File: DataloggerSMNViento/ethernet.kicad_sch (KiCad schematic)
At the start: 1 part

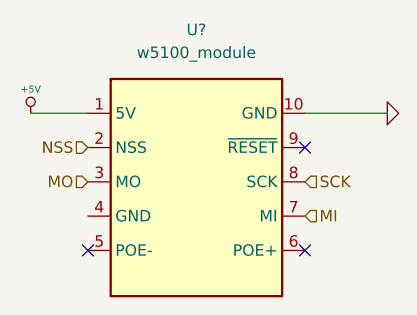
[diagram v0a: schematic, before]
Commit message: Agrego modificaciones al poncho de la EDU CIAA, también agrego una simulacion del circuito para tomar la tensión del ADC del tunnel
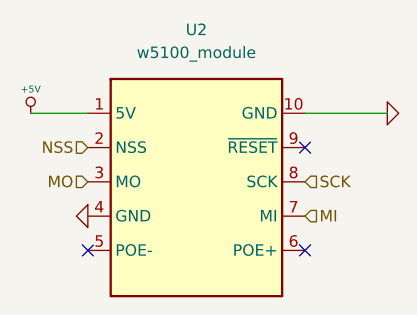
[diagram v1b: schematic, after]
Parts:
- U2: renamed from U?; footprint (none) -> Modulos:W5100_module
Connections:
- net GND: now also U2.4 (GND)
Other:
- company: (none) -> Servicio Meteorológico Nacional - FIUBA - UBA
- title: (none) -> Datalogger para SCTV
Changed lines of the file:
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@@
 (kicad_sch (version 20211123) (generator eeschema)
   (paper "A4")
+  (title_block
+    (title "Datalogger para SCTV")
+    (date "2023-10-20")
+    (rev "1.0")
+    (company "Servicio Meteorológico Nacional - FIUBA - UBA")
+    (comment 1 "poner repo")
+    (comment 2 "Autores y Licencia del poncho: Cristian Aranda (FIUBA), ver archivo licence.txt")
+    (comment 3 "Autor del poncho: Cristian Zozimo Aranda Cordero.  Ver directorio \"doc\"")
+    (comment 4 "CÓDIGO PONCHO: DT1")
+  )
   (no_connect (at 147.193 68.961))
   (no_connect (at 123.063 68.961))
@@
   (symbol (lib_id "Misc_Poncho_Grande:GND") (at 156.337 53.721 90) (unit 1)
     (in_bom yes) (on_board yes) (fields_autoplaced)
-    (property "Reference" "#PWR?" (id 0) (at 156.337 53.721 0)
+    (property "Reference" "#PWR014" (id 0) (at 156.337 53.721 0)
       (effects (font (size 0.762 0.762)) hide)
     )
@@
   (symbol (lib_id "New_Library:w5100_module") (at 134.493 76.581 0) (unit 1)
     (in_bom yes) (on_board yes) (fields_autoplaced)
-    (property "Reference" "U?" (id 0) (at 135.128 44.45 0))
+    (property "Reference" "U2" (id 0) (at 135.128 44.45 0))
     (property "Value" "w5100_module" (id 1) (at 135.128 46.99 0))
-    (property "Footprint" "" (id 2) (at 134.493 76.581 0)
+    (property "Footprint" "Modulos:W5100_module" (id 2) (at 134.493 76.581 0)
       (effects (font (size 1.27 1.27)) hide)
     )
@@
   (symbol (lib_id "Misc_Poncho_Grande:+5V") (at 116.713 53.721 0) (unit 1)
     (in_bom yes) (on_board yes) (fields_autoplaced)
-    (property "Reference" "#PWR?" (id 0) (at 116.713 51.435 0)
+    (property "Reference" "#PWR013" (id 0) (at 116.713 51.435 0)
       (effects (font (size 0.508 0.508)) hide)
     )
@@
       (effects (font (size 1.524 1.524)))
     )
+    (pin "1")
+  )
+  (symbol (lib_id "Misc_Poncho_Grande:GND") (at 123.063 65.151 270) (unit 1)
+    (in_bom yes) (on_board yes) (fields_autoplaced)
+    (property "Reference" "#PWR0102" (id 0) (at 123.063 65.151 0)
+      (effects (font (size 0.762 0.762)) hide)
+    )
+    (property "Value" "GND" (id 1) (at 121.285 65.151 0)
+      (effects (font (size 0.762 0.762)) hide)
+    )
+    (property "Footprint" "" (id 2) (at 123.063 65.151 0)
+      (effects (font (size 1.524 1.524)))
+    )
+    (property "Datasheet" "" (id 3) (at 123.063 65.151 0)
+      (effects (font (size 1.524 1.524)))
+    )

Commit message: Subo la version v1.0 del PCB del poncho de la tesis
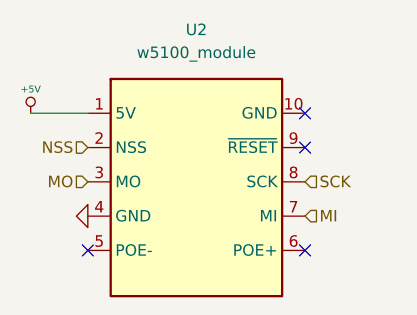
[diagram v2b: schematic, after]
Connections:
- net GND: no longer U2.10 (GND)
- no-connect marks 3 -> 4
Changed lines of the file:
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@@
   (no_connect (at 123.063 68.961))
   (no_connect (at 147.193 57.531))
-  (wire (pts (xy 147.193 53.721) (xy 156.337 53.721))
-    (stroke (width 0) (type default) (color 0 0 0 0))
-  )
+  (no_connect (at 147.193 53.721))
   (wire (pts (xy 116.713 53.721) (xy 123.063 53.721))
     (stroke (width 0) (type default) (color 0 0 0 0))
@@
     (effects (font (size 1.27 1.27)) (justify right))
   )
-  (symbol (lib_id "Misc_Poncho_Grande:GND") (at 156.337 53.721 90) (unit 1)
-    (in_bom yes) (on_board yes) (fields_autoplaced)
-    (property "Reference" "#PWR014" (id 0) (at 156.337 53.721 0)
-      (effects (font (size 0.762 0.762)) hide)
-    )
-    (property "Value" "GND" (id 1) (at 158.115 53.721 0)
-      (effects (font (size 0.762 0.762)) hide)
-    )
-    (property "Footprint" "" (id 2) (at 156.337 53.721 0)
-      (effects (font (size 1.524 1.524)))
-    )
-    (property "Datasheet" "" (id 3) (at 156.337 53.721 0)
-      (effects (font (size 1.524 1.524)))
-    )
-    (pin "1")
-  )
   (symbol (lib_id "New_Library:w5100_module") (at 134.493 76.581 0) (unit 1)
